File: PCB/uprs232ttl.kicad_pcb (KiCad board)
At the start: 2 copper layers, 44.7 x 48.8 mm, 13 parts, among them J1 RX Int, J2 Pwr, J3 Serial, J4 RX/TX, J5 CTS/RTS, U1 4050

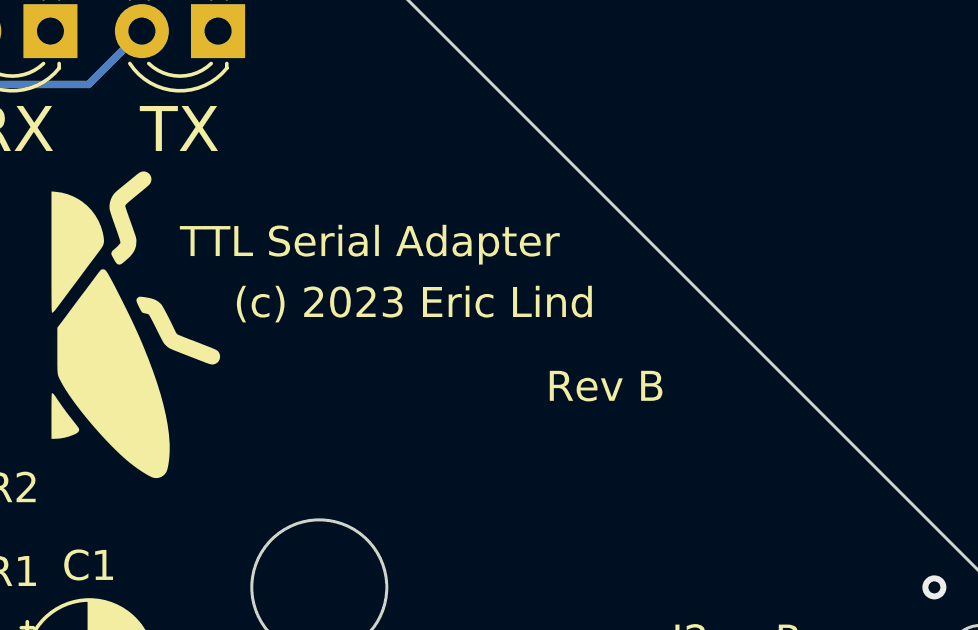
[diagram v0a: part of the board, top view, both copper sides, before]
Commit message: Updated board name
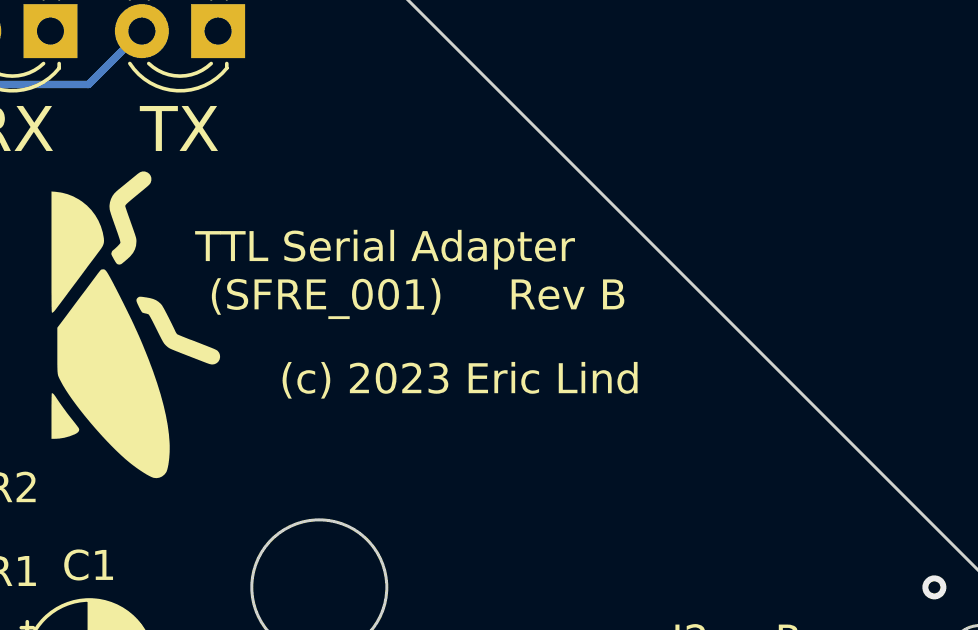
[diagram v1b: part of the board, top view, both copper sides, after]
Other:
- board text added: "TTL Serial Adapter (SFRE_001)"
- board text removed: "TTL Serial Adapter"
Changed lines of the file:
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@@
     (effects (font (size 1 1) (thickness 0.15)) (justify left bottom mirror))
   )
-  (gr_text "(c) 2023 Eric Lind" (at 149.86 89.916) (layer "F.SilkS")
+  (gr_text "(c) 2023 Eric Lind" (at 151.384 92.456) (layer "F.SilkS")
     (effects (font (size 1 1) (thickness 0.15)) (justify left bottom))
   )
@@
     (effects (font (size 1 1) (thickness 0.2) bold) (justify left bottom))
   )
-  (gr_text "Rev B" (at 160.274 92.71) (layer "F.SilkS")
+  (gr_text "Rev B" (at 159.004 89.662) (layer "F.SilkS")
     (effects (font (size 1 1) (thickness 0.15)) (justify left bottom))
   )
@@
     (effects (font (size 1 1) (thickness 0.2) bold) (justify left bottom))
   )
-  (gr_text "TTL Serial Adapter" (at 148.082 87.884) (layer "F.SilkS")
+  (gr_text "TTL Serial Adapter\n (SFRE_001)" (at 148.59 89.662) (layer "F.SilkS")
     (effects (font (size 1 1) (thickness 0.15)) (justify left bottom))
   )
